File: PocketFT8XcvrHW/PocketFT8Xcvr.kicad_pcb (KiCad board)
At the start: 4 copper layers, 100 x 69.9 mm, 62 parts, among them J1 HX8357D SPI, J2 22-23-2021, J3 B5B-XH-A_LF__SN_, J4 XMT PWR, J5 HX8357D 8-BIT, Q3 2N7000, U1 MCP3422A1T-E/SN, U2 Si4735-D60-GU, U3 SN74ACT244DWR, U4 SI5351C-B-GM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

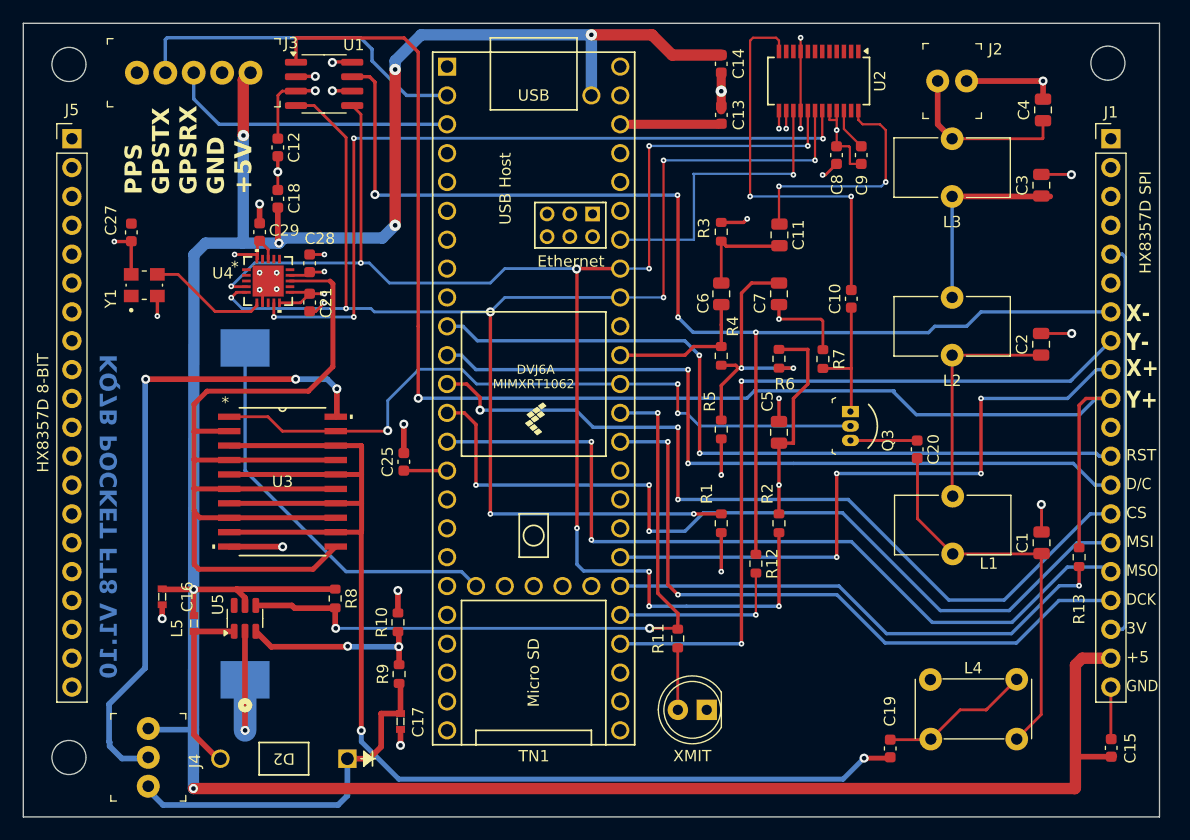
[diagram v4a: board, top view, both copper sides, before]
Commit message: Changed PA from MMIC to 74ACT244
New PA chip.
Optional step-up power supply apparently helps xmit power.
Connector for choosing PA power (5V or ~6.6V).
Misc bug fixes.
7-Pole LP filter (TODO:  Choose the real inductor/capacitor values).
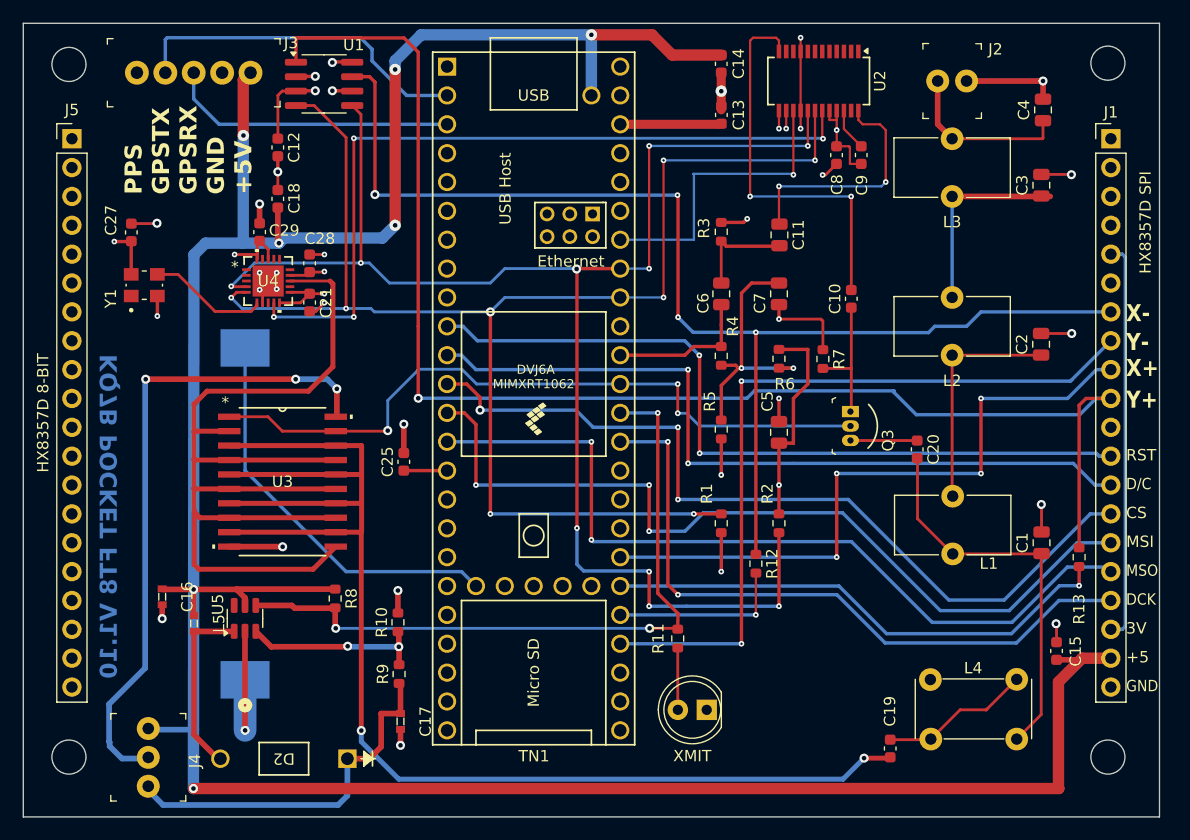
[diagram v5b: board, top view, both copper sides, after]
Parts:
- added REF**: MountingHole_3mm, MountingHole:MountingHole_3mm, F.Cu at (197.9, 115.4)
- moved C15 9.79 mm to (193.3, 106.0)
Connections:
- J5 pad 1: (no net) -> unconnected-(J5-Pin_1-Pad1)
- J5 pad 10: (no net) -> unconnected-(J5-Pin_10-Pad10)
- J5 pad 11: (no net) -> unconnected-(J5-Pin_11-Pad11)
- J5 pad 12: (no net) -> unconnected-(J5-Pin_12-Pad12)
- J5 pad 13: (no net) -> unconnected-(J5-Pin_13-Pad13)
- J5 pad 14: (no net) -> unconnected-(J5-Pin_14-Pad14)
- J5 pad 15: (no net) -> unconnected-(J5-Pin_15-Pad15)
- J5 pad 16: (no net) -> unconnected-(J5-Pin_16-Pad16)
- J5 pad 17: (no net) -> unconnected-(J5-Pin_17-Pad17)
- J5 pad 18: (no net) -> unconnected-(J5-Pin_18-Pad18)
- J5 pad 19: (no net) -> unconnected-(J5-Pin_19-Pad19)
- J5 pad 2: (no net) -> unconnected-(J5-Pin_2-Pad2)
- J5 pad 20: (no net) -> unconnected-(J5-Pin_20-Pad20)
- J5 pad 3: (no net) -> unconnected-(J5-Pin_3-Pad3)
- J5 pad 4: (no net) -> unconnected-(J5-Pin_4-Pad4)
- J5 pad 5: (no net) -> unconnected-(J5-Pin_5-Pad5)
- J5 pad 6: (no net) -> unconnected-(J5-Pin_6-Pad6)
- J5 pad 7: (no net) -> unconnected-(J5-Pin_7-Pad7)
- J5 pad 8: (no net) -> unconnected-(J5-Pin_8-Pad8)
- J5 pad 9: (no net) -> unconnected-(J5-Pin_9-Pad9)
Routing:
- net +5V: track 253.0 -> 251.4 mm
- net GND: track 94.1 -> 93.4 mm, vias 32 -> 34

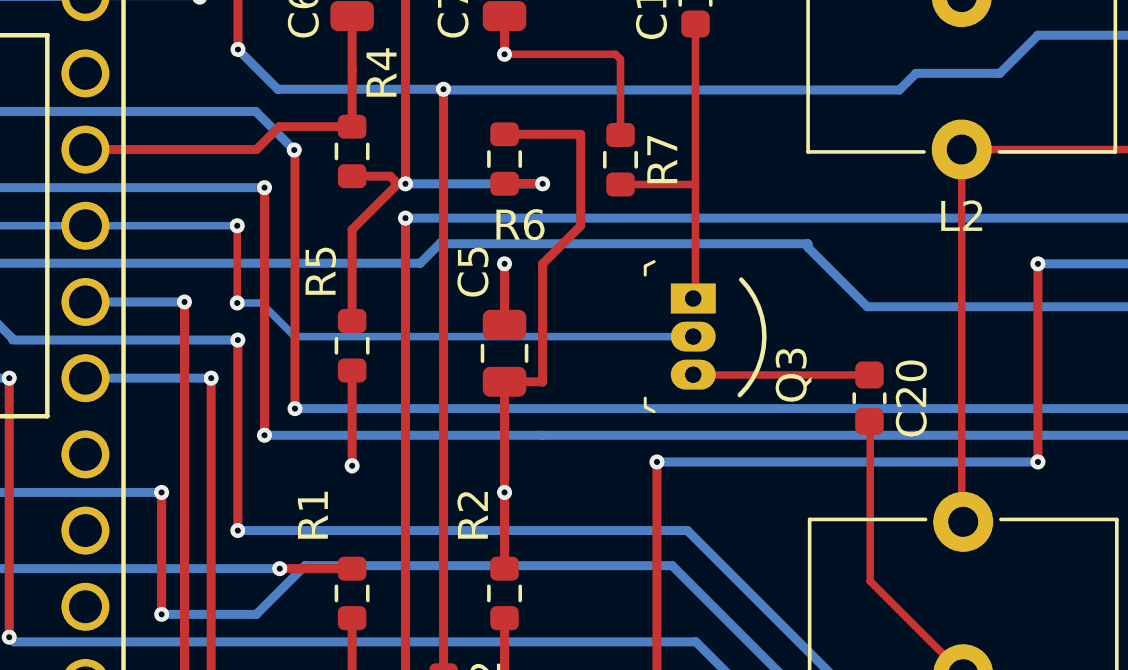
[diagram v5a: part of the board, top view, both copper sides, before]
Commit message: REPLACED the two 2N7000s with a dual mosfet, 2N7002DW
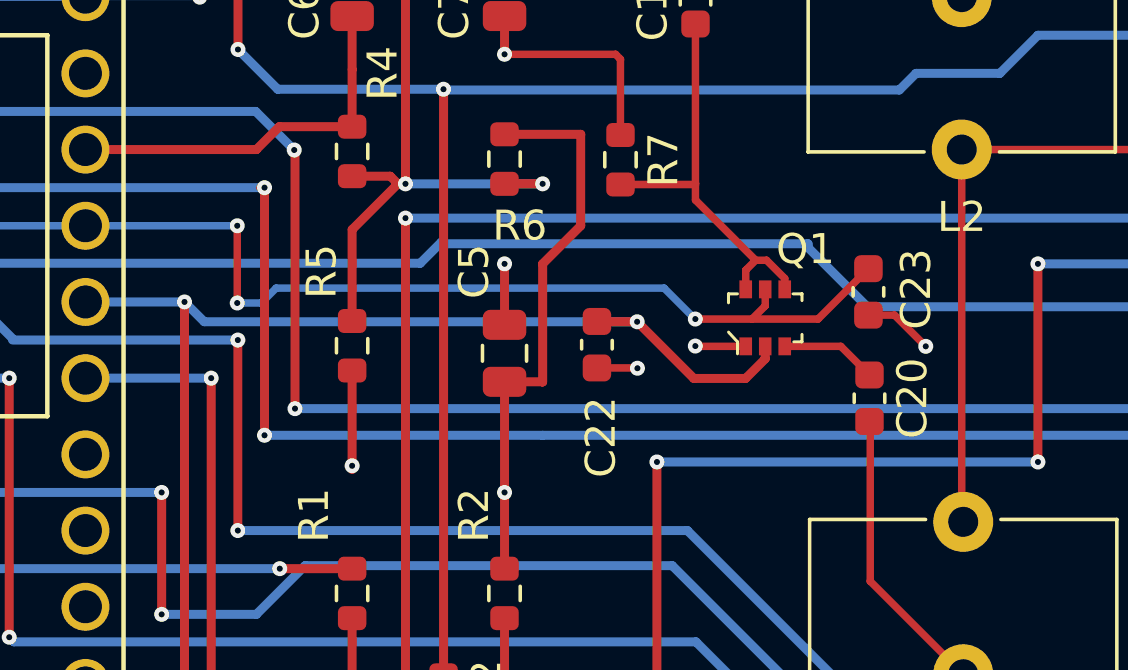
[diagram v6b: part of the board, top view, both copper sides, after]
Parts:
- removed Q3: 2N7000, digikey-footprints:TO-92-3
- added C22: 10nF, Capacitor_SMD:C_0603_1608Metric, F.Cu at (172.0, 86.5)
- added C23: 10nF, Capacitor_SMD:C_0603_1608Metric, F.Cu at (181.0, 84.8)
- added Q1: 2N7002DW, digikey-footprints:SOT-363, F.Cu at (177.6, 85.6)
- C1, C4: value 910pf -> 750 pF
- C2, C3: value 1300pf -> 1200 pF
- L1, L3: value 1.2uh -> 1.3 uH
- L2: value 1.2uh -> 1.5 uH
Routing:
- net /XMT: track 62.1 -> 84.6 mm, vias 3 -> 4
- net /RCV: track 62.8 -> 70.5 mm, vias 3 -> 4
- net GND: track 93.4 -> 98.8 mm, vias 34 -> 37
- net Net-(Q1-D1): track 5.70 -> 3.22 mm
- net Net-(Q1-D2): track 11.7 -> 13.9 mm

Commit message: Cleanup PCB
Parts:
- moved R2 31.8 mm to (163.8, 63.5)
- moved R1 30.1 mm to (171.5, 65.7)
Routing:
- net /SCL: track 135.9 -> 89.7 mm, vias 10 -> 5
- net /SDA: track 129.2 -> 93.4 mm, vias 8 -> 5
- net +3.3V: track 69.4 -> 72.6 mm, vias 8 -> 7
- net /+VPA: track 57.0 -> 55.7 mm
- net GND: track 98.8 -> 97.5 mm

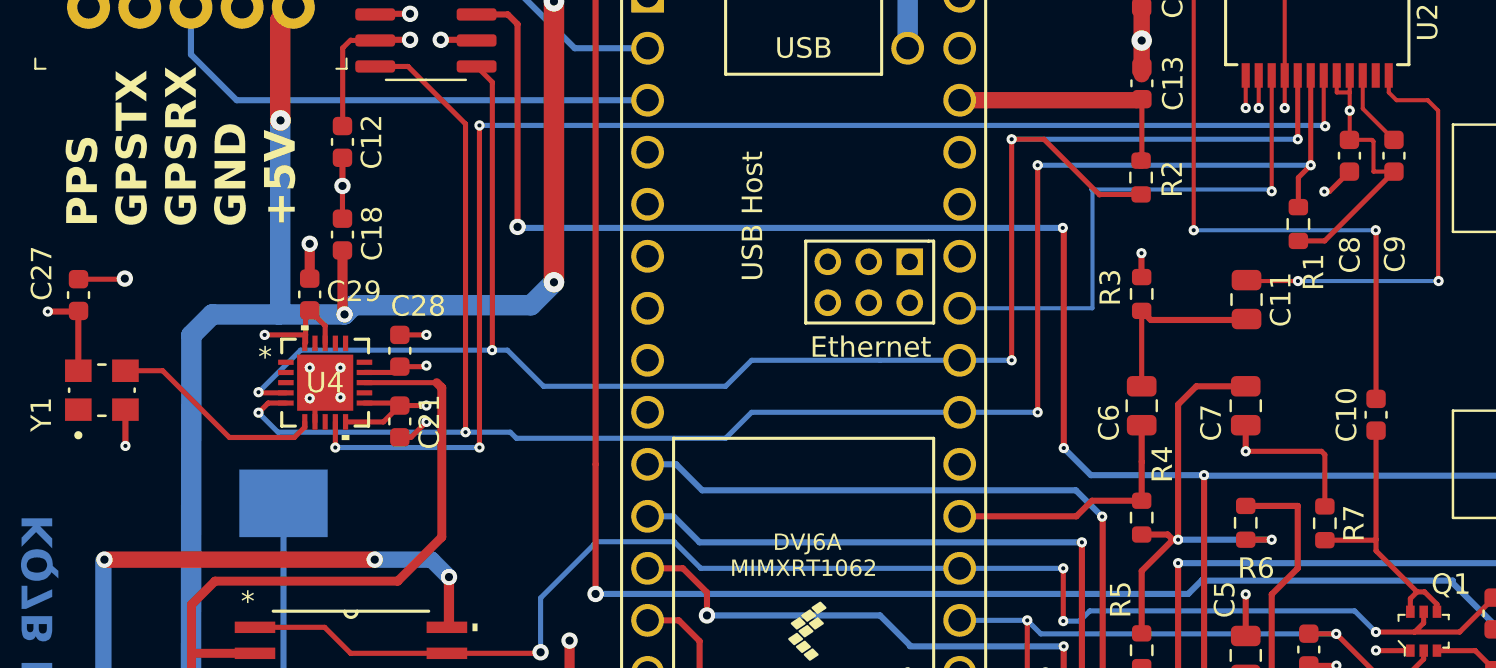
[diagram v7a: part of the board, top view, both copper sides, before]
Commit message: Added test points
Don't use sparkfun TPs again :(
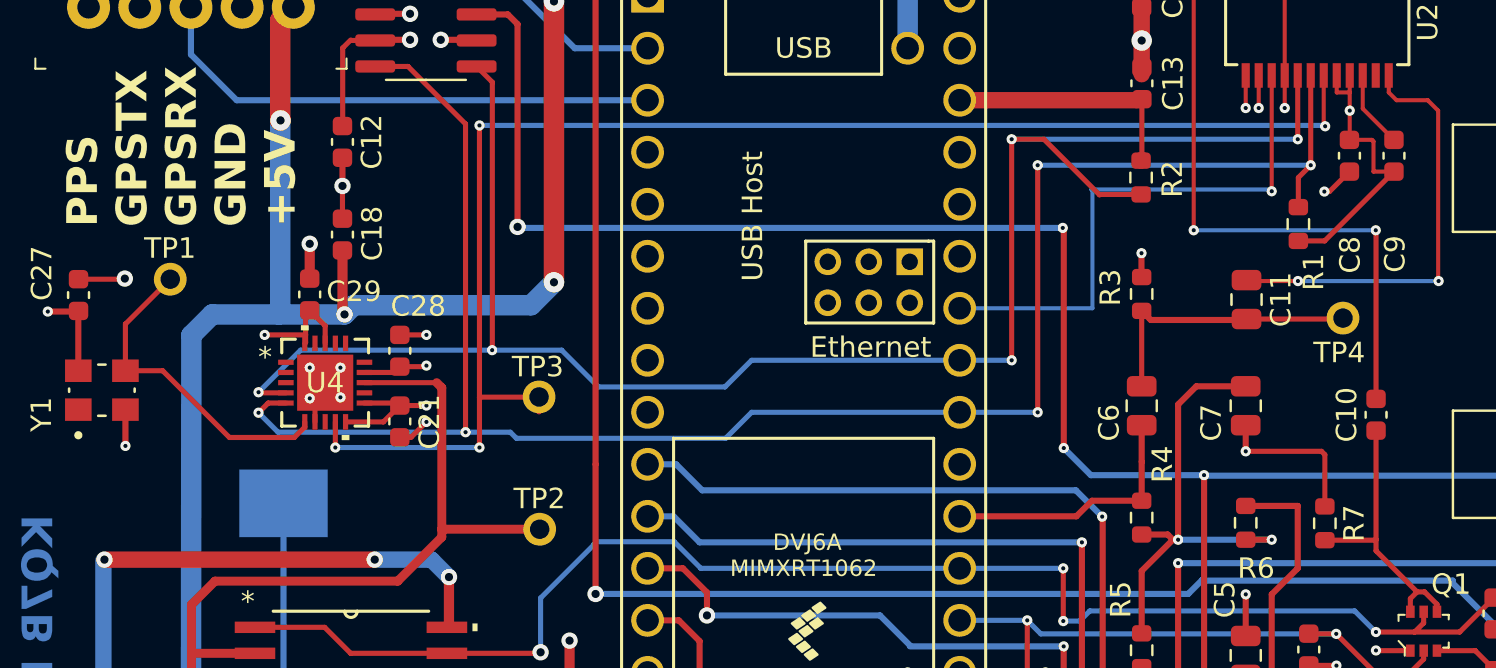
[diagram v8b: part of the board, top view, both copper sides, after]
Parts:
- added TP1: PTH, SparkFun-Connector:1x01, F.Cu at (116.4, 68.4)
- added TP2: PTH, SparkFun-Connector:1x01, F.Cu at (134.4, 80.6)
- added TP3: PTH, SparkFun-Connector:1x01, F.Cu at (134.4, 74.2)
- added TP4: PTH, SparkFun-Connector:1x01, F.Cu at (173.7, 70.3)
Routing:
- net Net-(U4-CLKIN): track 10.6 -> 15.9 mm
- net Net-(C11-Pad2): track 8.95 -> 14.0 mm
- net /XCLK: track 93.2 -> 98.0 mm
- net /RCLK: track 67.8 -> 71.1 mm
